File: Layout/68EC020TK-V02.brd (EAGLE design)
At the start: 124.9 x 100 mm, 100 parts, among them IC10 74HCT245PW, IC11 74HCT245PW, IC12 AM29F010S, IC13 XC95288XL-TQ144, IC14 ICS570B, IC15 74HCT245PW, IC2 MC68EC020RP, IC3 74ACT16245, IC4 74ACT16245, IC5 LD117AS33TR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

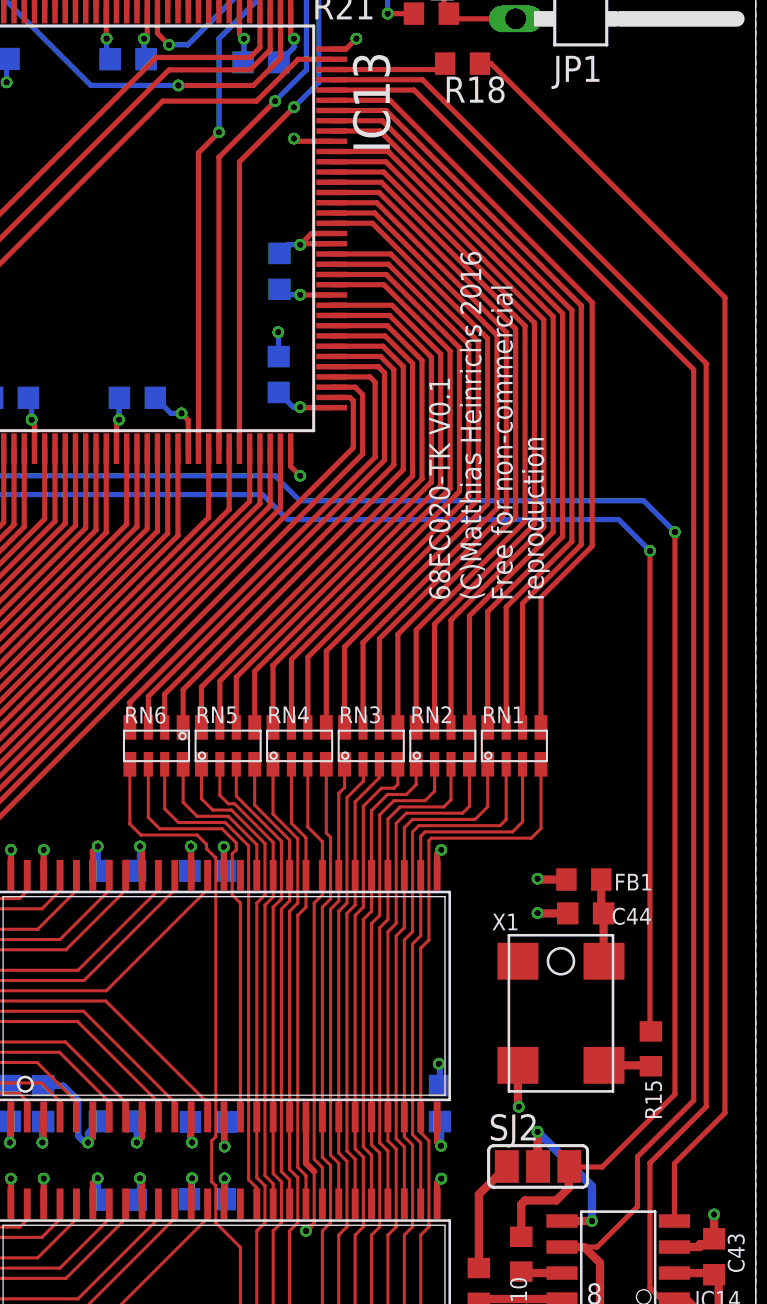
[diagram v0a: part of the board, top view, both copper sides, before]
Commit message: Adjusted resistor nets
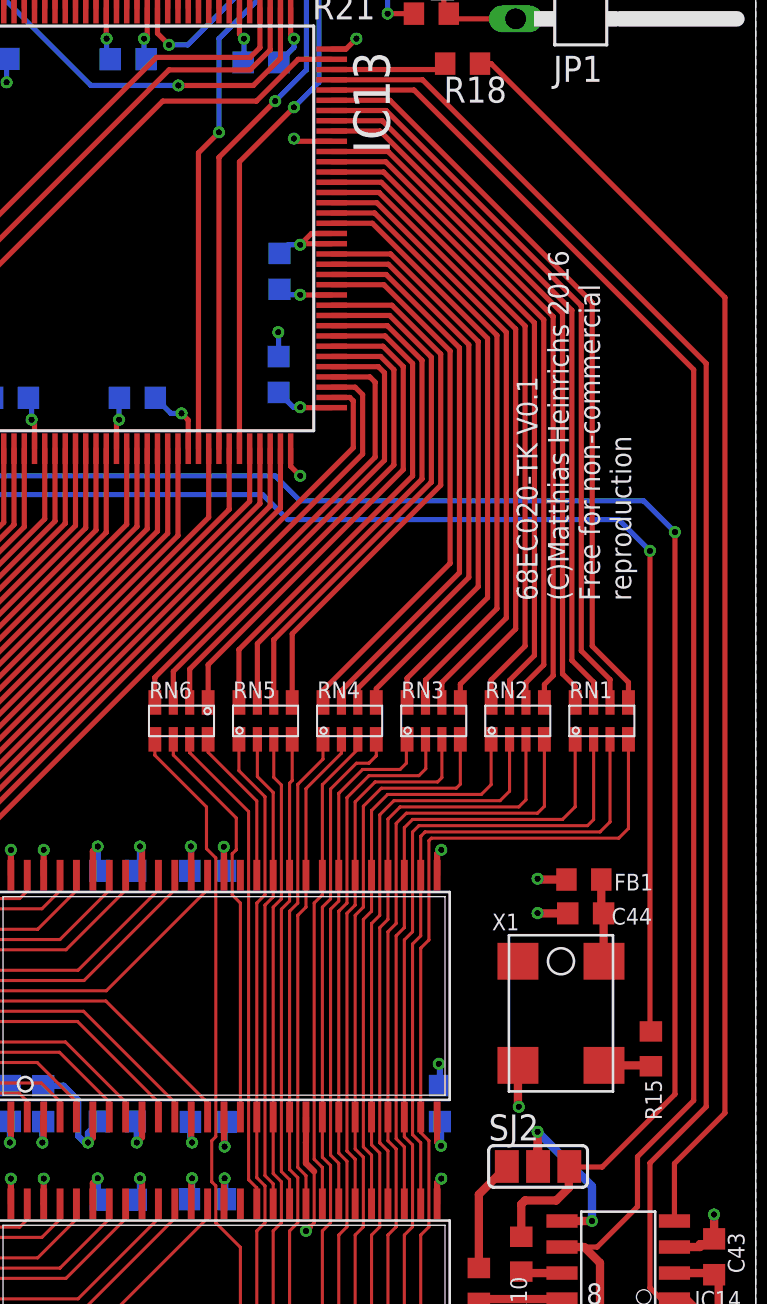
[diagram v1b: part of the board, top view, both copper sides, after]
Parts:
- moved RN1 4.44 mm to (117.4, 41.7)
- moved RN2 3.86 mm to (113.3, 41.7)
- moved RN3 3.28 mm to (109.2, 41.7)
- moved RN4 2.73 mm to (105.1, 41.7)
- moved RN5 2.20 mm to (101.0, 41.7)
- moved RN6 1.72 mm to (96.9, 41.7)
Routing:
- net ARAM_5: track 25.2 -> 30.7 mm
- net ARAM_3: track 38.9 -> 44.4 mm
- net ARAM_2: track 38.0 -> 43.4 mm
- net ARAM_4: track 26.3 -> 31.8 mm
- net ARAM_7: track 23.2 -> 28.1 mm
- net ARAM_6: track 24.3 -> 29.2 mm
- net ARAM_1: track 36.8 -> 41.7 mm
- net ARAM_0: track 35.7 -> 40.6 mm
- net ARAM_10: track 34.8 -> 39.1 mm
- net ARAM_8: track 22.3 -> 26.5 mm
- net BA1: track 34.1 -> 38.0 mm
- net ARAM_9: track 21.9 -> 25.4 mm
- net C_ARAM_6: track 35.3 -> 32.6 mm
- net C_ARAM_0: track 34.7 -> 32.0 mm
- net C_ARAM_7: track 34.1 -> 31.4 mm
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
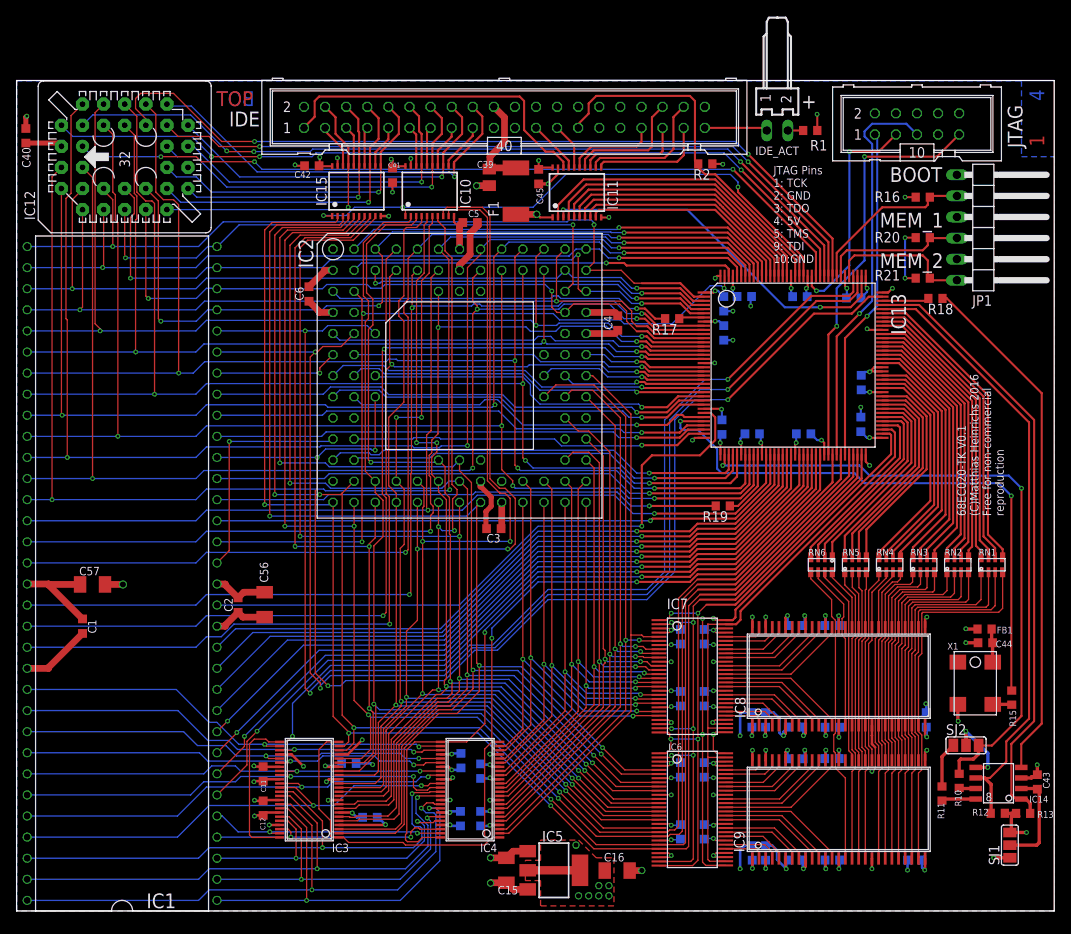
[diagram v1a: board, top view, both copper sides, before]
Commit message: fixed parts but mem cfg not bug free
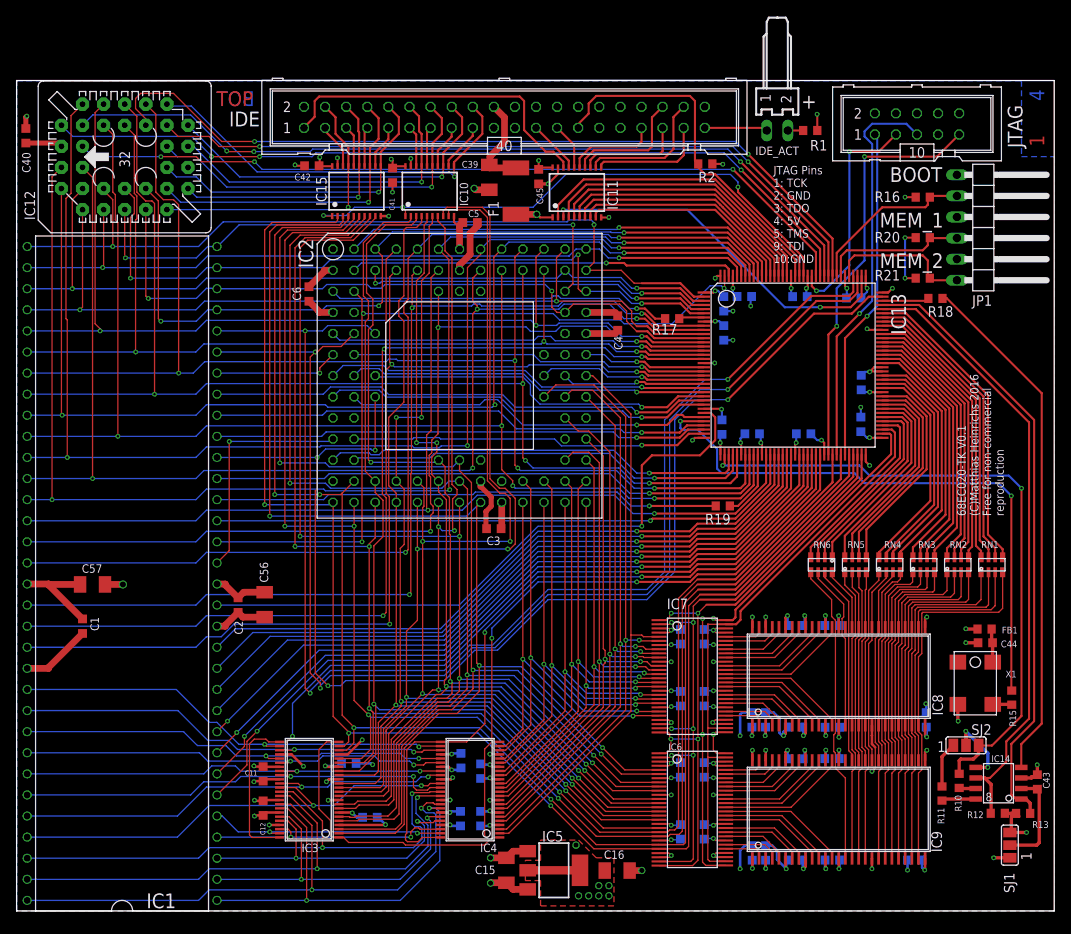
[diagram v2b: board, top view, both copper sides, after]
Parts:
- C24, C25, C26, C27, C28, C29, C30, C31: value 10nF -> 100nF
- C39: value 47µF -> 47uF; device rcl:C0805K -> rcl:C1206K
- C43, C44: value (none) -> 100nF
- FB1: value 100Ohm@100MHz -> 120Ohm@100MHz 0.5A
- IC12: value AM29F010S -> AM29F010S-10
- IC13: value XC95288XL-TQ144 -> XC95288XL-TQ144-10ns
- IC6, IC7: value 74ALVT16543 -> 74LVT16543
- IC8, IC9: value K4S56163 -> AS4C4M16SA-6TCN
- X1: value (none) -> 16,66MHz / 3.3V

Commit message: Improved layout
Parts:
- added R3, R4: n.b., rcl:R0603
- C44: value 100nF -> n.b.
- FB1: value 120Ohm@100MHz 0.5A -> n.b.
- IC14: value ICS570B -> ICS570A
- IC5: value LD117AS33TR -> LD117ADT33TR; device v-reg:SOT223 -> v-reg:DPACK
- R15: value 33 -> n.b.
- X1: value 16,66MHz / 3.3V -> n.b.
- moved C15 4.57 mm to (54.4, 4.90)
- moved SJ1 3.48 mm to (119.5, 4.45), turned to 0 degrees
- moved IC5 1.83 mm to (62.9, 4.90)
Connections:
- net +3V3: no longer IC5.2
- net +5V: no longer R12.2, R13.2
- net GND: now also R3.1, R4.1
- net S0: now also R4.2
- net S1: now also R3.2
- net VCC_IC14: now also R12.2, R13.2
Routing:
- net VCC_IC14: track 12.2 -> 22.3 mm
- net +5V: track 100.4 -> 96.5 mm
- net +3V3: track 92.6 -> 89.5 mm, vias 41 -> 44
- net GND: track 237.8 -> 240.9 mm, vias 84 -> 86
- net S0: track 75.5 -> 77.2 mm
- net S1: track 74.2 -> 75.7 mm
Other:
- board text added: "3.3V 5V"
